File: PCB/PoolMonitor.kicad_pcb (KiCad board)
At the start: 4 copper layers, 48.6 x 34.3 mm, 19 parts, among them J1 Conn_01x02_Male, J2 Conn_01x06_Female, J3 Conn_01x02_Male, J4 Conn_01x02_Male, Q1 DMP2225L-7, Q2 AO3400A, U2 ESP-12E

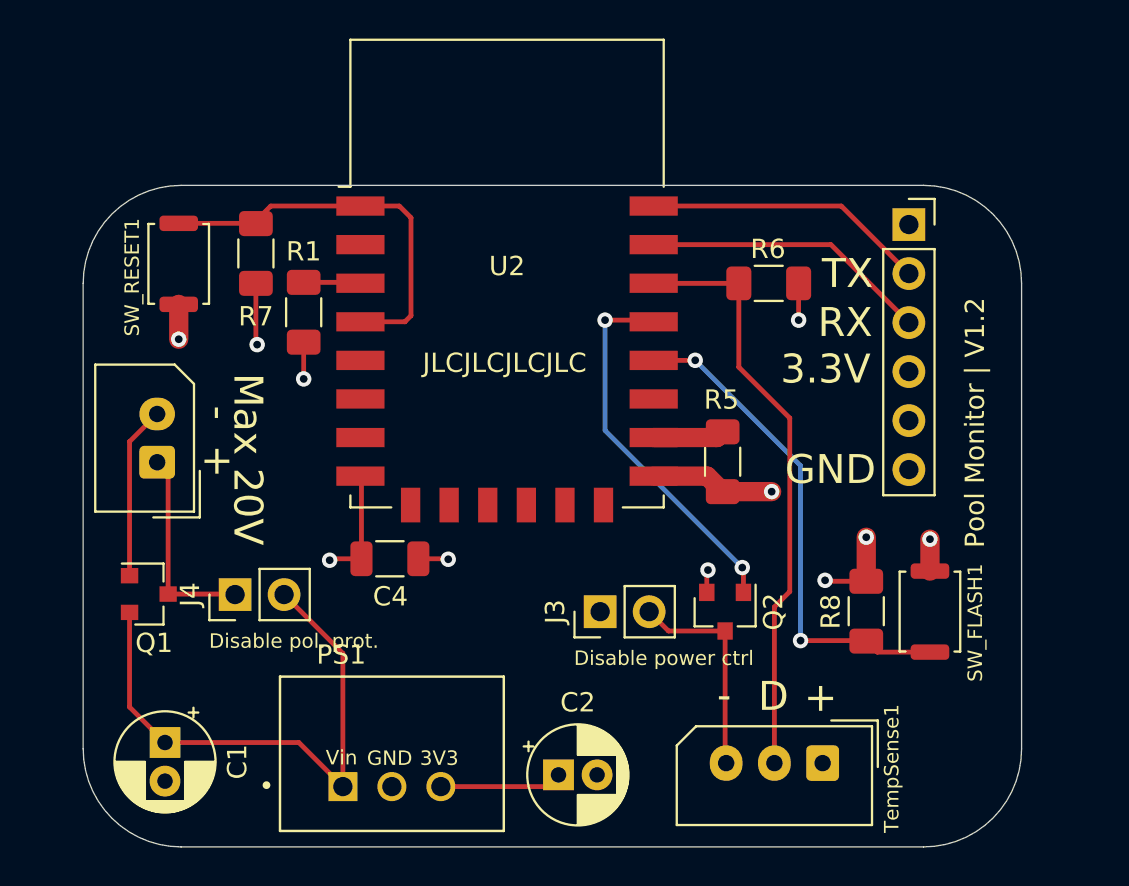
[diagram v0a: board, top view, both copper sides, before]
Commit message: Updated PCB and software to be able to read battery voltage as well as added solar charging capabilities to PCB
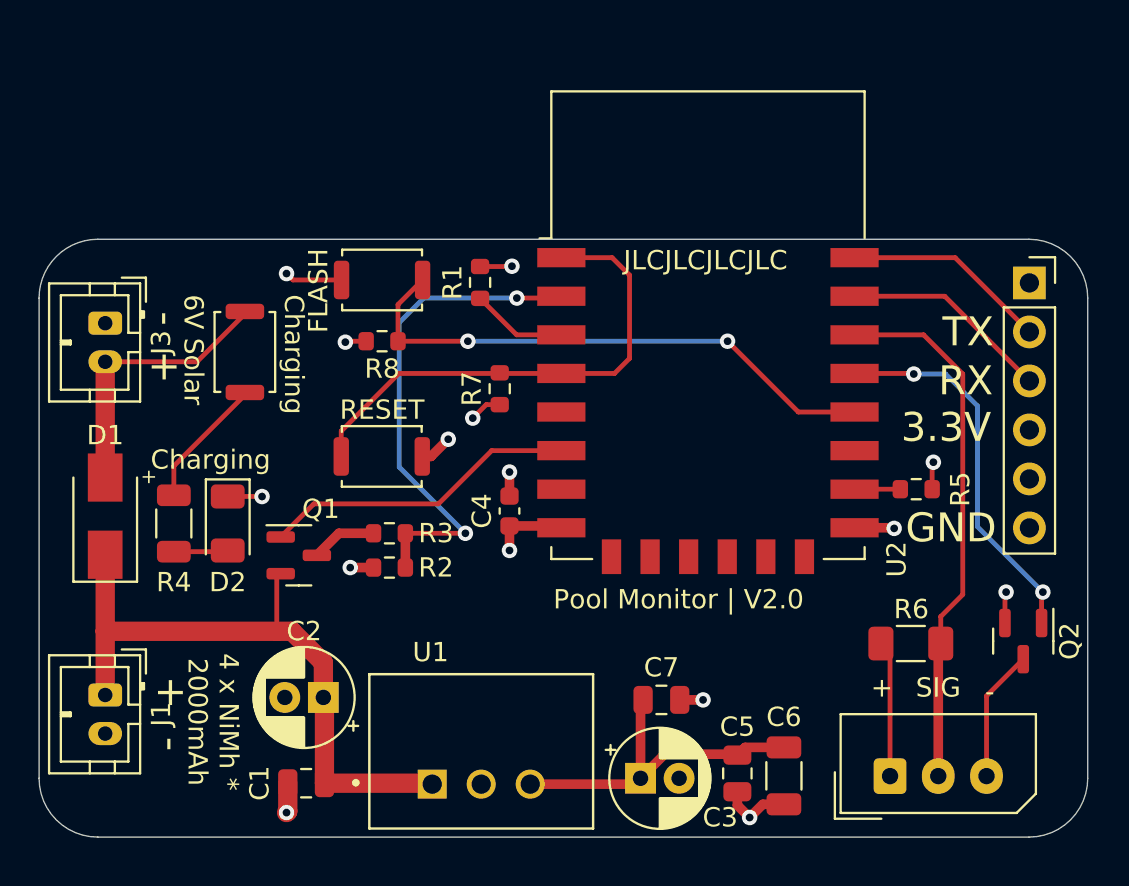
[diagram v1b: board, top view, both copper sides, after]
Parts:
- removed J4: Conn_01x02_Male, Connector_PinHeader_2.54mm:PinHeader_1x02_P2.54mm_Vertical
- removed PS1: K7803M-1000R3, CustomFootprints:CONV_K7803M-1000R3
- added C3: 22uF, Capacitor_THT:CP_Radial_D5.0mm_P2.00mm, F.Cu at (52.5, 51.1)
- added C5: 10uF, Capacitor_SMD:C_0805_2012Metric, F.Cu at (57.5, 50.8)
- added C6: 4.7uF, Capacitor_SMD:C_1206_3216Metric, F.Cu at (59.9, 50.9)
- added C7: 100nF, Capacitor_SMD:C_0805_2012Metric, F.Cu at (53.6, 47.0)
- added CHK_CHARGE1: SW_Push, Button_Switch_SMD:SW_Push_SPST_NO_Alps_SKRK, F.Cu at (32.0, 29.0)
- added D1: SS14, Diode_SMD:D_SMA, F.Cu at (24.8, 37.5)
- added D2: LED_GREEN, LED_SMD:LED_1206_3216Metric, F.Cu at (31.1, 37.8)
- added R2: 2K, Resistor_SMD:R_0603_1608Metric, F.Cu at (39.5, 40.1)
- added R3: 10K, Resistor_SMD:R_0603_1608Metric, F.Cu at (39.5, 38.4)
- added R4: 1K, Resistor_SMD:R_1206_3216Metric, F.Cu at (28.3, 37.8)
- added U1: K7803M-1000R3, CustomFootprints:CONV_K7803M-1000R3, F.Cu at (44.3, 49.7)
- C1: footprint Capacitor_THT:CP_Radial_D5.0mm_P2.00mm -> Capacitor_SMD:C_0805_2012Metric
- C4: footprint Capacitor_SMD:C_1206_3216Metric -> Capacitor_SMD:C_0603_1608Metric
- J1: footprint Connector_Molex:Molex_SPOX_5267-02A_1x02_P2.50mm_Vertical -> Connector_JST:JST_PH_B2B-PH-K_1x02_P2.00mm_Vertical
- J3: value Conn_01x02_Male -> SolarPanel6V; footprint Connector_PinHeader_2.54mm:PinHeader_1x02_P2.54mm_Vertical -> Connector_JST:JST_PH_B2B-PH-K_1x02_P2.00mm_Vertical
- R1, R5, R7, R8: footprint Resistor_SMD:R_1206_3216Metric_Pad1.30x1.75mm_HandSolder -> Resistor_SMD:R_0603_1608Metric
- moved SW_FLASH1 33.2 mm to (39.1, 25.2), turned to 180 degrees
- moved J3 29.7 mm to (24.8, 27.5), turned to -90 degrees
- moved R8 28.7 mm to (39.1, 28.4), turned to 180 degrees
- moved R6 20.1 mm to (66.5, 44.1), turned to 180 degrees
- moved Q2 15.5 mm to (72.4, 43.9)
- moved SW_RESET1 14.5 mm to (39.1, 34.4), turned to 0 degrees
- moved R7 14.5 mm to (45.2, 30.9)
- moved C2 12.8 mm to (36.1, 46.9), turned to 180 degrees
- moved J1 12.4 mm to (24.8, 46.7), turned to -90 degrees
- moved U2 10.8 mm to (56.0, 27.6)
- moved R5 10.1 mm to (66.8, 36.1), turned to 180 degrees
- moved R1 9.27 mm to (44.2, 25.4), turned to 90 degrees
- moved Q1 8.03 mm to (34.8, 39.5)
- moved C1 7.61 mm to (35.2, 51.3), turned to 0 degrees
- moved J2 6.94 mm to (72.7, 25.4)
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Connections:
- C1 pad 1: +BATT -> GND
- C1 pad 2: GND -> +BATT
- C2 pad 1: +3V3 -> +BATT
- J1 pad 1: Net-(J1-Pad1) -> +BATT
- J2 pad 1: (no net) -> unconnected-(J2-Pad1)
- J2 pad 5: (no net) -> unconnected-(J2-Pad5)
- J3 pad 2: TempSenseGND -> PV+
- Q1 pad 1: GND -> PowerCheckControl
- Q1 pad 3: Net-(J1-Pad1) -> Net-(Q1-Pad3)
- U2 pad 10: (no net) -> unconnected-(U2-Pad10)
- U2 pad 11: (no net) -> unconnected-(U2-Pad11)
- U2 pad 12: (no net) -> unconnected-(U2-Pad12)
- U2 pad 13: (no net) -> unconnected-(U2-Pad13)
- U2 pad 14: (no net) -> unconnected-(U2-Pad14)
- U2 pad 17: (no net) -> unconnected-(U2-Pad17)
- U2 pad 2: (no net) -> Power_ADC
- U2 pad 5: (no net) -> unconnected-(U2-Pad5)
- U2 pad 6: (no net) -> PowerCheckControl
- U2 pad 7: (no net) -> unconnected-(U2-Pad7)
- U2 pad 9: (no net) -> unconnected-(U2-Pad9)
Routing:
- net Power_ADC: track 0.00 -> 26.2 mm, vias 0 -> 2
- net PowerCheckControl: track 0.00 -> 16.4 mm
- net PV+: track 0.00 -> 14.3 mm
- net Net-(J1-Pad1): track 10.5 -> 0.00 mm
- net +3V3: track 23.8 -> 33.6 mm, vias 6 -> 4
- net Net-(CHK_CHARGE1-Pad2): track 0.00 -> 6.73 mm
- net +BATT: track 28.9 -> 34.5 mm
- net RST_IN: track 20.6 -> 26.0 mm
- net TempSenseGND: track 11.2 -> 6.85 mm
- net RX_IN: track 14.7 -> 10.7 mm
- net TX_IN: track 14.9 -> 10.9 mm
- net Net-(Q1-Pad3): track 0.00 -> 3.41 mm
- net GPIO0_IN: track 25.9 -> 28.9 mm
- net TempSenseIn: track 30.7 -> 27.8 mm
- net Net-(D2-Pad2): track 0.00 -> 2.82 mm
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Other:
- board size 48.6 x 34.3 mm -> 54.4 x 31 mm
- board text added: "4 x NiMh * 2000mAh"
- board text added: "6V Solar"
- board text added: "Charging"
- board text added: "FLASH"
- board text added: "Pool Monitor | V2.0"
- board text added: "RESET"
- board text added: "SIG"
- board text removed: "3V3"
- board text removed: "D"
- board text removed: "Disable pol. prot."
- board text removed: "Disable power ctrl"
- board text removed: "Max 20V"
- board text removed: "Pool Monitor | V1.2"
- board text removed: "Vin"

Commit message: Updated to use all JST connectors and updated REAME with a description
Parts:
- TempSense1: footprint Connector_Molex:Molex_SPOX_5267-03A_1x03_P2.50mm_Vertical -> Connector_JST:JST_PH_B3B-PH-K_1x03_P2.00mm_Vertical
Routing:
- net +3V3: track 33.6 -> 34.3 mm
